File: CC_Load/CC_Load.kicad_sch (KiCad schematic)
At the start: 57 parts, among them J1 VoltSense_Conn, J2 PowerInput_Conn, J3 LED_Conn, J4 Load_Conn, J5 16x2_LCD_Conn, J6 RotEnc_Conn, J7 Fan_Conn, Q1 IRLZ44N, Q2 IRLZ44N, Q3 IRLZ44N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

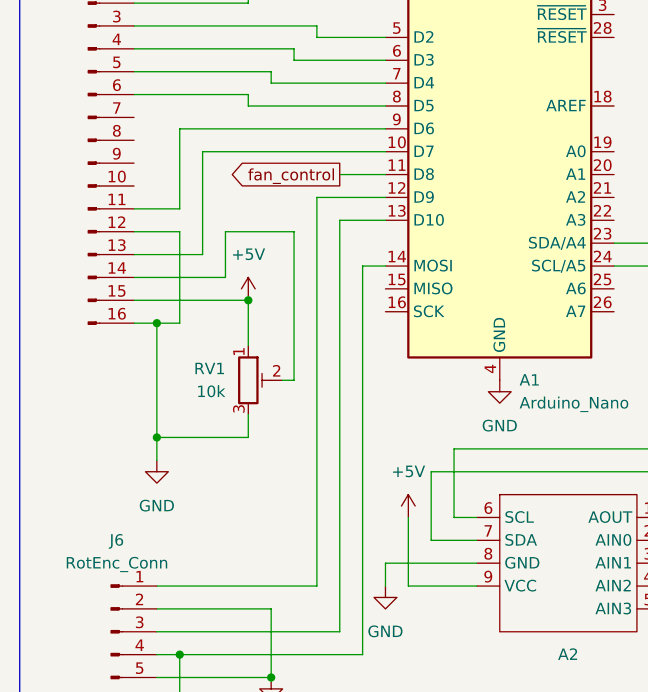
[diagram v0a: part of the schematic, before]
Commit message: Finished first design for my DIY PCB
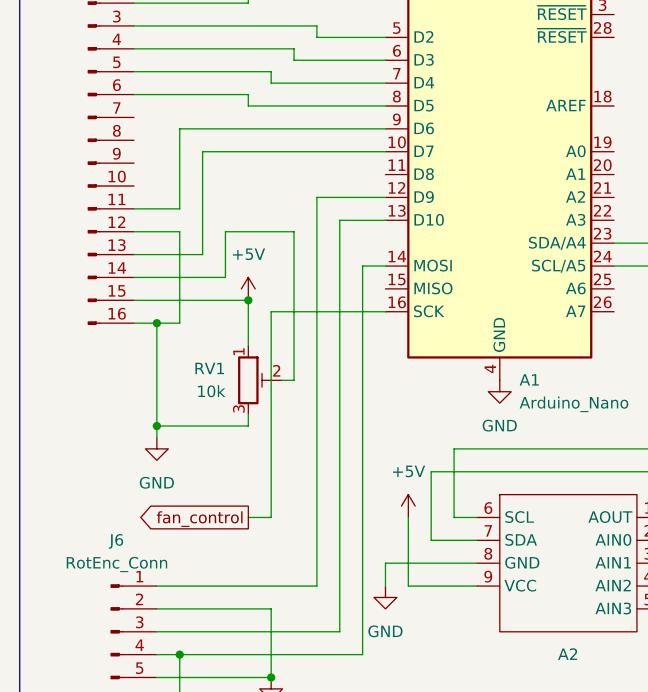
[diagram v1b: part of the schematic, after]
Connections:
- net fan_control: now also A1.16 (SCK); no longer A1.11 (D8)
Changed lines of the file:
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@@
   (junction (at 190.5 114.3) (diameter 0) (color 0 0 0 0)
   )
-  (junction (at 33.02 135.89) (diameter 0) (color 0 0 0 0)
+  (junction (at 33.02 134.62) (diameter 0) (color 0 0 0 0)
   )
   (junction (at 236.22 91.44) (diameter 0) (color 0 0 0 0)
@@
     (stroke (width 0) (type default))
   )
-  (wire (pts (xy 33.02 135.89) (xy 33.02 123.19))
+  (wire (pts (xy 33.02 134.62) (xy 33.02 123.19))
     (stroke (width 0) (type default))
   )
@@
     (stroke (width 0) (type default))
   )
+  (wire (pts (xy 43.18 144.78) (xy 45.72 144.78))
+    (stroke (width 0) (type default))
+  )
   (wire (pts (xy 35.56 38.1) (xy 35.56 50.8))
     (stroke (width 0) (type default))
@@
     (stroke (width 0) (type default))
   )
-  (wire (pts (xy 43.18 133.35) (xy 43.18 135.89))
+  (wire (pts (xy 43.18 133.35) (xy 43.18 134.62))
     (stroke (width 0) (type default))
   )
@@
     (stroke (width 0) (type default))
   )
+  (wire (pts (xy 45.72 144.78) (xy 45.72 121.92))
+    (stroke (width 0) (type default))
+  )
   (wire (pts (xy 83.82 114.3) (xy 93.98 114.3))
     (stroke (width 0) (type default))
@@
     (stroke (width 0) (type default))
   )
-  (wire (pts (xy 53.34 106.68) (xy 58.42 106.68))
-    (stroke (width 0) (type default))
-  )
   (wire (pts (xy 33.02 160.02) (xy 35.56 160.02))
     (stroke (width 0) (type default))
@@
     (stroke (width 0) (type default))
   )
-  (wire (pts (xy 43.18 135.89) (xy 33.02 135.89))
+  (wire (pts (xy 43.18 134.62) (xy 33.02 134.62))
     (stroke (width 0) (type default))
   )
@@
     (stroke (width 0) (type default))
   )
-  (wire (pts (xy 33.02 138.43) (xy 33.02 135.89))
+  (wire (pts (xy 33.02 135.89) (xy 33.02 134.62))
     (stroke (width 0) (type default))
   )
@@
   )
   (wire (pts (xy 83.82 78.74) (xy 88.9 78.74))
+    (stroke (width 0) (type default))
+  )
+  (wire (pts (xy 45.72 121.92) (xy 58.42 121.92))
     (stroke (width 0) (type default))
   )
@@
     (effects (font (size 1.27 1.27)) (justify left bottom))
   )
-  (global_label "fan_control" (shape output) (at 53.34 106.68 180) (fields_autoplaced)
+  (global_label "fan_control" (shape output) (at 43.18 144.78 180) (fields_autoplaced)
     (effects (font (size 1.27 1.27)) (justify right))
-    (property "Intersheetrefs" "${INTERSHEET_REFS}" (at 39.6508 106.68 0)
+    (property "Intersheetrefs" "${INTERSHEET_REFS}" (at 29.4908 144.78 0)
       (effects (font (size 1.27 1.27)) (justify right) hide)
     )
@@
     )
   )
-  (symbol (lib_id "power:GND") (at 33.02 138.43 0) (unit 1)
-    (in_bom yes) (on_board yes) (dnp no) (fields_autoplaced)
-    (property "Reference" "#PWR015" (at 33.02 144.78 0)
-      (effects (font (size 1.27 1.27)) hide)
-    )
-    (property "Value" "GND" (at 33.02 143.51 0)
-      (effects (font (size 1.27 1.27)))
-    )
-    (property "Footprint" "" (at 33.02 138.43 0)
-      (effects (font (size 1.27 1.27)) hide)
-    )
-    (property "Datasheet" "" (at 33.02 138.43 0)
-      (effects (font (size 1.27 1.27)) hide)
-    )
+  (symbol (lib_id "power:GND") (at 33.02 135.89 0) (unit 1)
+    (in_bom yes) (on_board yes) (dnp no) (fields_autoplaced)
+    (property "Reference" "#PWR015" (at 33.02 142.24 0)
+      (effects (font (size 1.27 1.27)) hide)
+    )
+    (property "Value" "GND" (at 33.02 140.97 0)
+      (effects (font (size 1.27 1.27)))
+    )
+    (property "Footprint" "" (at 33.02 135.89 0)
+      (effects (font (size 1.27 1.27)) hide)
+    )
+    (property "Datasheet" "" (at 33.02 135.89 0)
+      (effects (font (size 1.27 1.27)) hide)
+    )

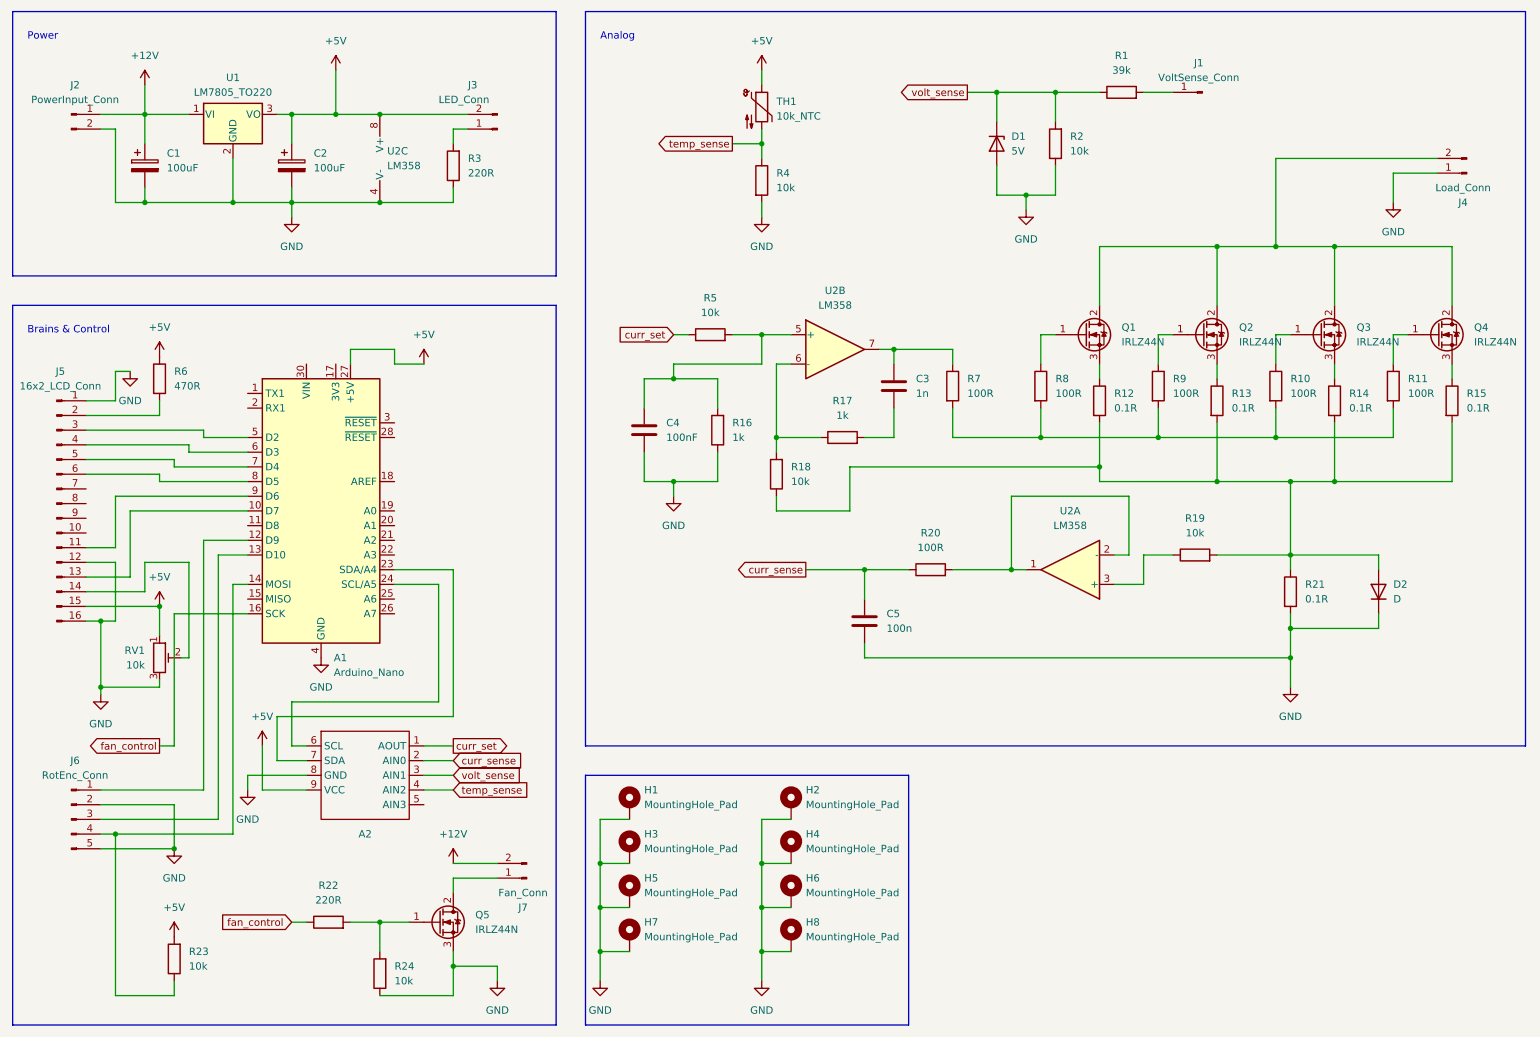
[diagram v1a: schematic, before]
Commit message: Changed PCB design, will order from JLCPCB
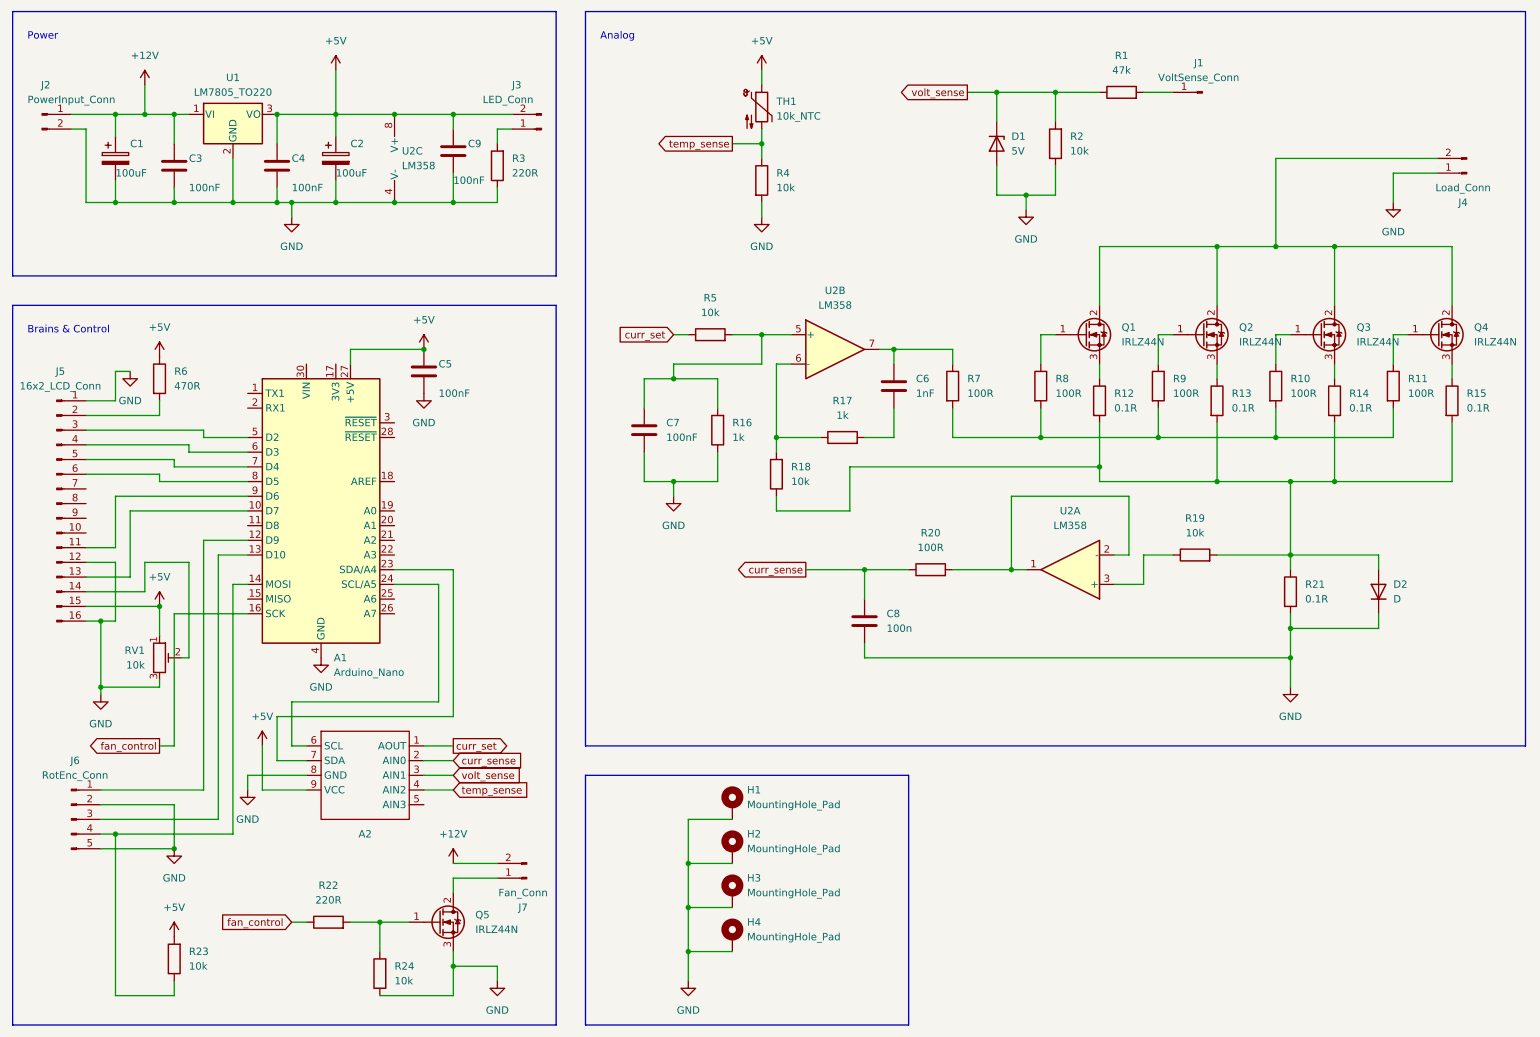
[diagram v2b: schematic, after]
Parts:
- removed H1, H3, H5, H7: MountingHole_Pad, MountingHole:MountingHole_3.2mm_M3_Pad, symbol Mechanical:MountingHole_Pad
- added C3, C4, C5, C9: 100nF, Capacitor_SMD:C_1206_3216Metric, symbol Device:C
- C6: renamed from C3; value 1n -> 1nF; footprint Capacitor_THT:C_Disc_D3.4mm_W2.1mm_P2.50mm -> Capacitor_SMD:C_1206_3216Metric
- C7: renamed from C4; footprint Capacitor_THT:C_Disc_D3.4mm_W2.1mm_P2.50mm -> Capacitor_SMD:C_1206_3216Metric
- C8: renamed from C5; footprint Capacitor_THT:C_Disc_D3.4mm_W2.1mm_P2.50mm -> Capacitor_SMD:C_1206_3216Metric
- R1: value 39k -> 47k; footprint Resistor_THT:R_Axial_DIN0204_L3.6mm_D1.6mm_P7.62mm_Horizontal -> Resistor_SMD:R_1206_3216Metric
- R10, R11, R16, R17, R18, R19, R2, R20, R22, R23, R24, R3, R4, R5, R6, R7, R8, R9: footprint Resistor_THT:R_Axial_DIN0204_L3.6mm_D1.6mm_P7.62mm_Horizontal -> Resistor_SMD:R_1206_3216Metric
- renumbered H2 to H1, H4 to H2, H6 to H3, H8 to H4
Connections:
- net +12V: now also C3.1
- net +5V: now also C4.1, C5.1, C9.1
- net GND: now also C3.2, C4.2, C5.2, C9.2
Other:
- moved on the sheet: C1, C2, H1, H2, H3, H4, J2, J3, R3, U2C
